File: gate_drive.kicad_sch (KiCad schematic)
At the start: 108 parts, among them M1A1 HIGHCURRENTPAD2, M1B1 HIGHCURRENTPAD2, M1C1 HIGHCURRENTPAD2, M2A1 HIGHCURRENTPAD2, M2B1 HIGHCURRENTPAD2, M2C1 HIGHCURRENTPAD2, U1 EG2131, U14 CC6920B, U2 EG2131, U20 CC6920B, U22 CC6920B, U3 CC6920B, U4 EG2131, U5 EG2131, U7 EG2131, U8 EG2131

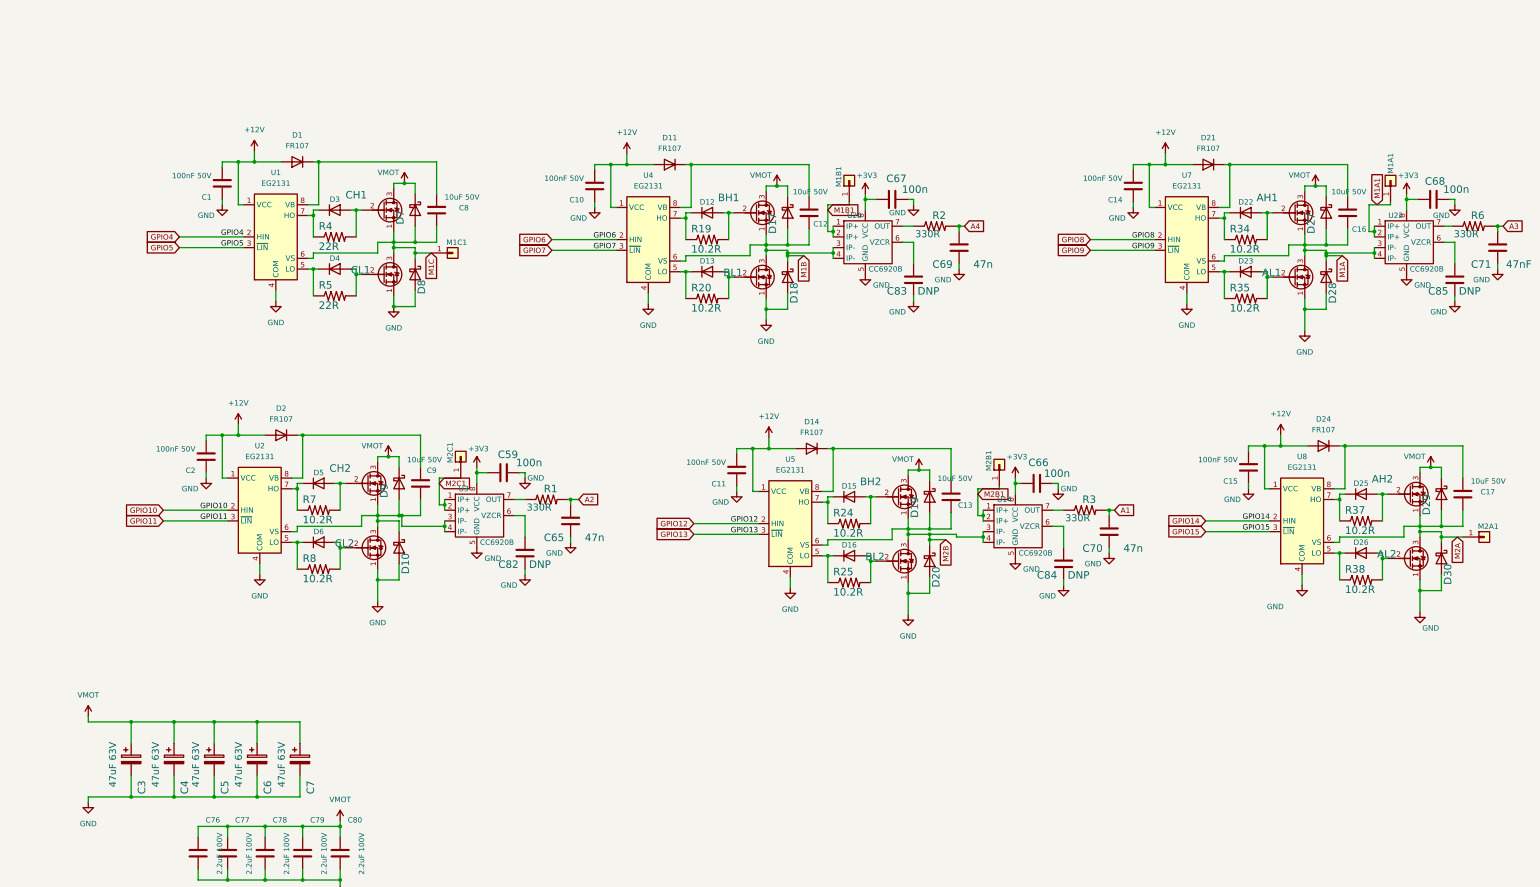
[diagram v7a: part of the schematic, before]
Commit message: Update dual CPU board to rev 2, ready for design review.
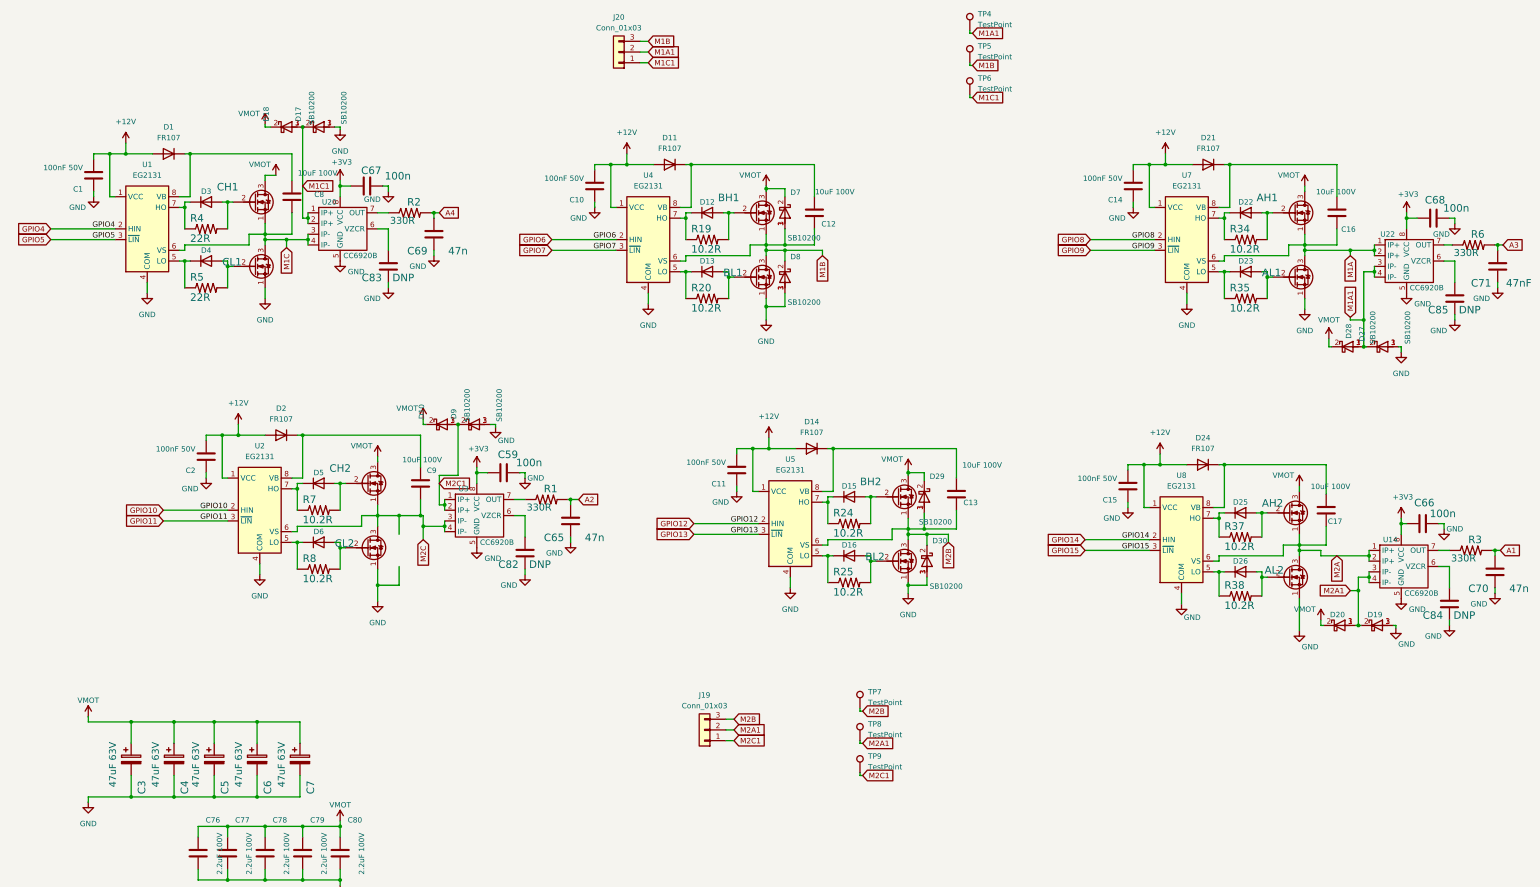
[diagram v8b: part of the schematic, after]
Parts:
- removed D10, D17, D18, D19, D20, D27, D28, D29, D30, D7, D8, D9: B5819W SL, Diode_SMD:D_SOD-123, symbol Diode:MBR340
- removed M1A1, M1B1, M1C1, M2A1, M2B1, M2C1: HIGHCURRENTPAD2, RP2040_minimal:PAD_12GA_WIRE, symbol Connector_Generic:Conn_01x01
- added D10, D17, D18, D19, D20, D27, D28, D29, D30, D7, D8, D9: SB10200, parts:TO-277_SB10200, symbol motor_parts:D_Schottky_AKA
- added J19, J20: Conn_01x03, parts:MT60-F.G.Y, symbol Connector_Generic:Conn_01x03
- added TP4, TP5, TP6, TP7, TP8, TP9: TestPoint, TestPoint:TestPoint_Pad_D3.0mm, symbol Connector:TestPoint
- C12, C13, C16, C17, C8, C9: value 10uF 50V -> 10uF 100V; footprint Capacitor_SMD:C_0805_2012Metric -> Capacitor_SMD:C_2220_5650Metric; LCSC C440198 -> C2843466
- U1, U2, U4, U5, U7, U8: LCSC C193777 -> C5240691
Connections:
- net M2B1 is gone; now on net M2A: U14.1 (IP+), U14.2 (IP+)
- net GND: now also D17.1 (A), D17.3 (A), D19.1 (A), D19.3 (A), D27.1 (A), D27.3 (A), D30.1 (A), D30.3 (A), D8.1 (A), D8.3 (A), D9.1 (A), D9.3 (A)
- net M1A: now also U22.1 (IP+), U22.2 (IP+); no longer U22.3 (IP-), U22.4 (IP-)
- net M1A1: now also U22.3 (IP-), U22.4 (IP-), D27.2 (K), D28.1 (A), D28.3 (A), J20.2 (Pin_2), TP4.1; no longer U22.1 (IP+), U22.2 (IP+)
- net M1B: now also D7.1 (A), D7.3 (A), D8.2 (K), J20.3 (Pin_3), TP5.1; no longer U20.3 (IP-), U20.4 (IP-)
- net M1C: now also U20.3 (IP-), U20.4 (IP-)
- net M2B: now also D29.1 (A), D29.3 (A), D30.2 (K), J19.3 (Pin_3), TP7.1; no longer U14.3 (IP-), U14.4 (IP-)
- net M2C1: now also D10.1 (A), D10.3 (A), D9.2 (K), J19.1 (Pin_1), TP9.1
- net VMOT: now also D10.2 (K), D18.2 (K), D20.2 (K), D28.2 (K), D29.2 (K), D7.2 (K)
- net M2C: now reaches C9.1, CH2.1 (S), CL2.3 (D), U2.6 (VS), U3.3 (IP-), U3.4 (IP-)
- net M1B1 renamed M1C1
- net M1C1: now also D17.2 (K), D18.1 (A), D18.3 (A), J20.1 (Pin_1), TP6.1
- new net M2A1: D19.2 (K), D20.1 (A), D20.3 (A), J19.2 (Pin_2), TP8.1, U14.3 (IP-), U14.4 (IP-)
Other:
- moved on the sheet: AH2, AL2, C1, C12, C13, C15, C16, C17, C66, C67, C68, C69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
